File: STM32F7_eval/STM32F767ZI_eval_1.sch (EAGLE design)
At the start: 101 parts, among them CN3 GROVE-4P-CONN-I2C-90D, CN4 GROVE-4P-CONN-AN01-90D, CN5 ARDUINO_COMPAT_IF, CN6 STLINKV21_SWD_IF, CN7 WFT0750CZ09-SMD_, CN8 MCO_IF, CN9 UART_IF, Q1 PMF370XN_, SW1 SKRPACE010_, SW2 SKRPACE010_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

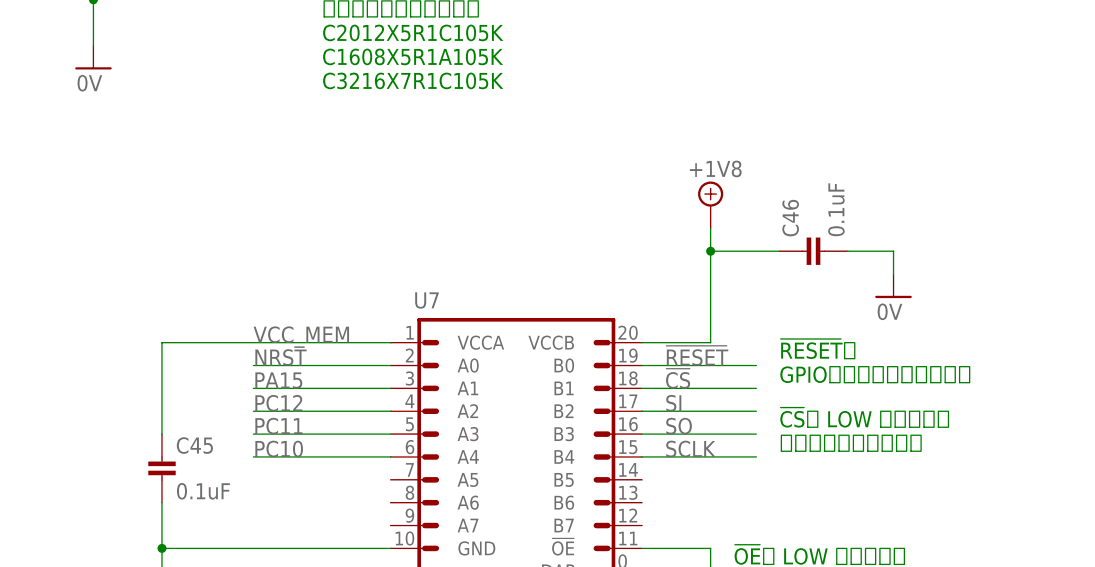
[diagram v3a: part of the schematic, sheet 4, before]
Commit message: 評価回路を修正
・コメント修正
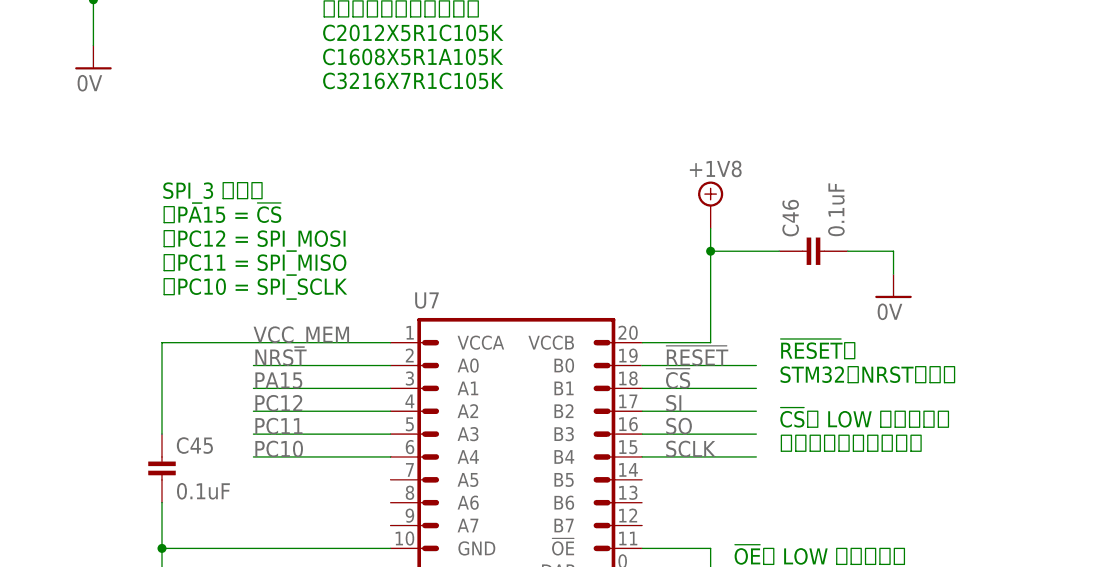
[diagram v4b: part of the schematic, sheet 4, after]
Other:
- note added: "!RESET!は STM32のNRSTに接続"
- note added: "I2C_2 を使用 ・PB10 = I2C_SCL ・PB11 = I2C_SDA"
- note added: "SPI_3 を使用 ・PA15 = !CS! ・PC12 = SPI_MOSI ・PC11 = SPI_MISO ・PC10 = SPI_SCLK"
- note removed: "!RESET!は GPIOを使用しても制御可能"
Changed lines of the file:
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@@
 <setting verticaltext="up"/>
 </settings>
-<grid distance="0.1" unitdist="inch" unit="inch" style="lines" multiple="1" display="no" altdistance="0.01" altunitdist="inch" altunit="inch"/>
+<grid distance="0.1" unitdist="inch" unit="inch" style="lines" multiple="1" display="yes" altdistance="0.01" altunitdist="inch" altunit="inch"/>
 <layers>
 <layer number="1" name="Top" color="4" fill="1" visible="no" active="no"/>
@@
 2.9inch - 1uF</text>
 <text x="101.6" y="165.1" size="2.54" layer="91">EPD接続インターフェース回路図</text>
+<text x="111.76" y="22.86" size="1.778" layer="91" align="top-left">I2C_2 を使用
+・PB10 = I2C_SCL
+・PB11 = I2C_SDA
+</text>
 </plain>
 <instances>
@@
 フラッシュが使用可能</text>
 <text x="200.66" y="83.82" size="1.778" layer="91" align="top-left">!RESET!は
-GPIOを使用しても制御可能</text>
+STM32のNRSTに接続</text>
 <text x="195.58" y="60.96" size="1.778" layer="91" align="top-left">!OE!に LOW を出力時は
 FXMA108のバスが
@@
 C3216X7R1C105K </text>
 <text x="104.14" y="160.02" size="2.54" layer="91">フラッシュメモリー回路図</text>
+<text x="132.08" y="101.6" size="1.778" layer="91" align="top-left">SPI_3 を使用
+・PA15 = !CS!
+・PC12 = SPI_MOSI
+・PC11 = SPI_MISO
+・PC10 = SPI_SCLK
+</text>
 </plain>
 <instances>

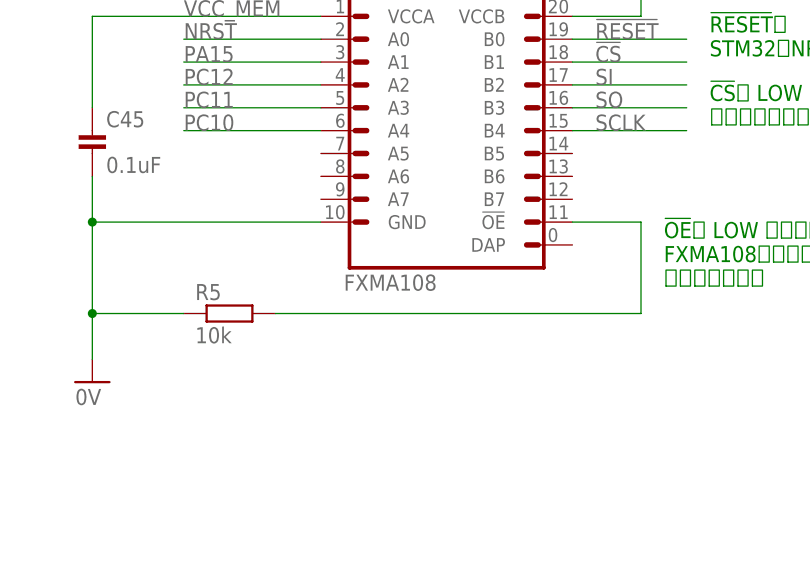
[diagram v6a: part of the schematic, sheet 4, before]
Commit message: 評価回路を修正
・手はんだパターンに置換え
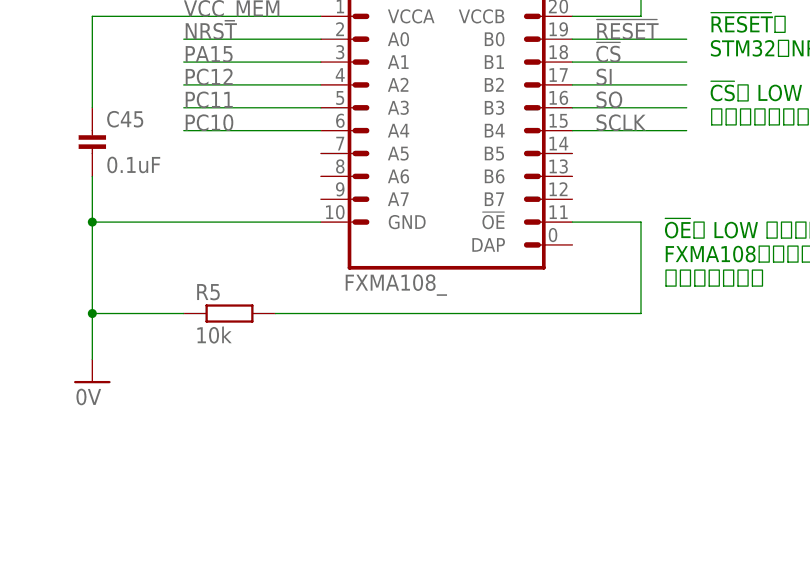
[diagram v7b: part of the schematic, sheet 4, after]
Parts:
- U7: value FXMA108 -> FXMA108_; device Parts:FXMA108 -> Parts:FXMA108_
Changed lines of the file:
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@@
 <part name="GND18" library="Supply" deviceset="0V" device=""/>
 <part name="C42" library="Parts" deviceset="CAP" device="_0603_DEV" value="0.1uF"/>
-<part name="U7" library="Parts" deviceset="FXMA108" device=""/>
+<part name="U7" library="Parts" deviceset="FXMA108" device="_" value="FXMA108_"/>
 <part name="SUPPLY1" library="PartsForProto" deviceset="+1V8" device=""/>
 <part name="SUPPLY2" library="PartsForProto" deviceset="+1V8" device=""/>

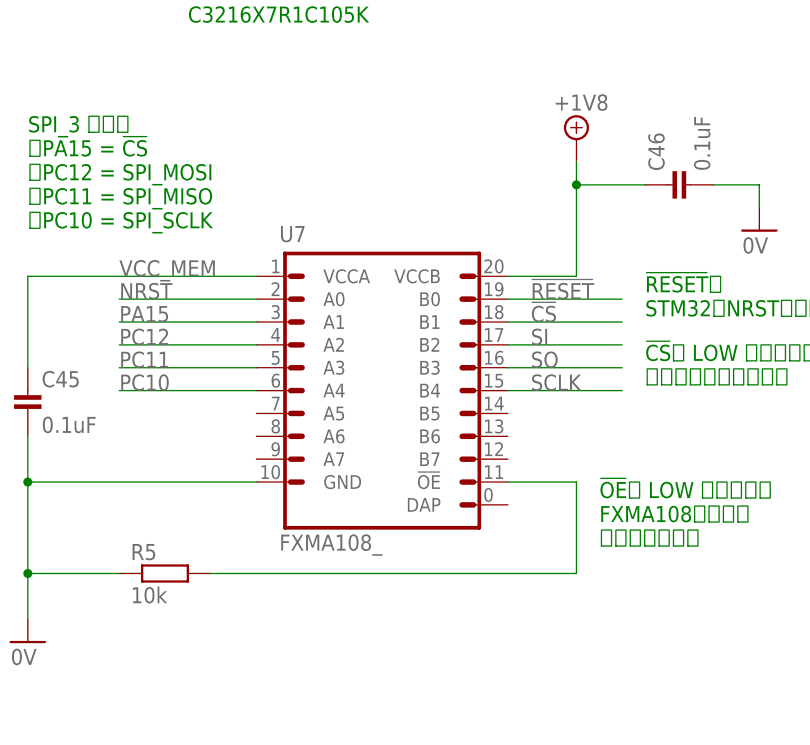
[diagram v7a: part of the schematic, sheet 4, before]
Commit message: 評価回路を修正
・配線を修正
・+1V8のNAMEが不正だったので修正
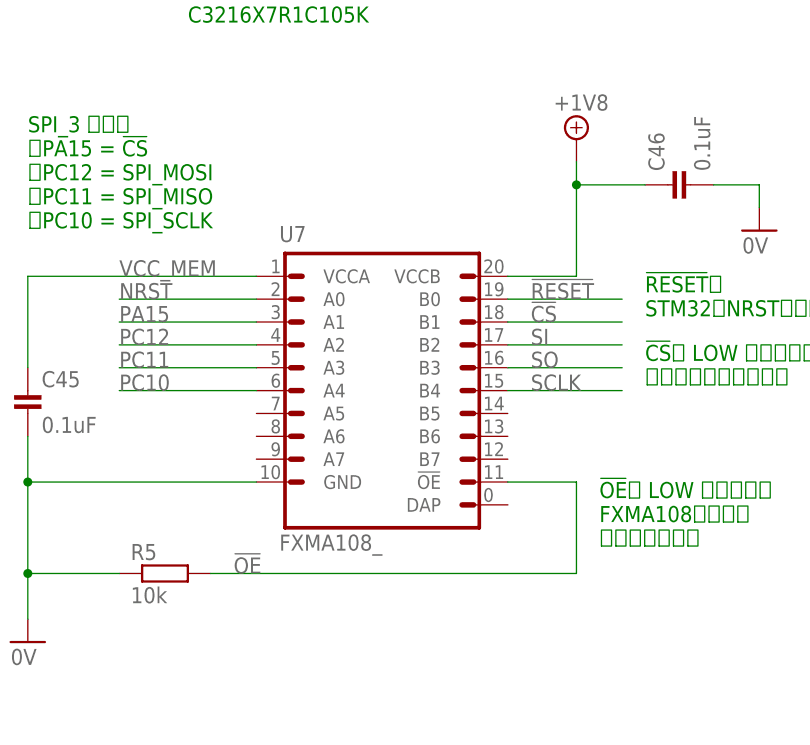
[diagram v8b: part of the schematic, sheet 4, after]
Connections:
- net +18V renamed +1V8
- net N$15 renamed !OE!
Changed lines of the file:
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@@
 <part name="C42" library="Parts" deviceset="CAP" device="_0603_DEV" value="0.1uF"/>
 <part name="U7" library="Parts" deviceset="FXMA108" device="_" value="FXMA108_"/>
-<part name="SUPPLY1" library="PartsForProto" deviceset="+1V8" device=""/>
-<part name="SUPPLY2" library="PartsForProto" deviceset="+1V8" device=""/>
+<part name="SUPPLY1" library="Supply" deviceset="+1V8" device=""/>
 <part name="GND20" library="Supply" deviceset="0V" device=""/>
-<part name="SUPPLY3" library="PartsForProto" deviceset="+1V8" device=""/>
+<part name="SUPPLY3" library="Supply" deviceset="+1V8" device=""/>
 <part name="GND21" library="Supply" deviceset="0V" device=""/>
 <part name="U8" library="Parts" deviceset="NCP563" device=""/>
@@
 <part name="+3V4" library="Supply" deviceset="+3V3" device=""/>
 <part name="R26" library="Parts" deviceset="RESISTOR" device="_0603_DEV" value="0"/>
+<part name="SUPPLY2" library="Supply" deviceset="+1V8" device=""/>
 </parts>
 <sheets>
@@
 <instance part="C42" gate="G$1" x="93.98" y="63.5"/>
 <instance part="U7" gate="G$1" x="157.48" y="83.82"/>
-<instance part="SUPPLY1" gate="+18V" x="93.98" y="93.98"/>
-<instance part="SUPPLY2" gate="+18V" x="193.04" y="99.06"/>
+<instance part="SUPPLY1" gate="G$1" x="93.98" y="93.98"/>
 <instance part="GND20" gate="1" x="132.08" y="43.18"/>
-<instance part="SUPPLY3" gate="+18V" x="147.32" y="149.86"/>
+<instance part="SUPPLY3" gate="G$1" x="147.32" y="149.86"/>
 <instance part="GND21" gate="1" x="124.46" y="114.3"/>
 <instance part="U8" gate="G$1" x="116.84" y="144.78"/>
@@
 <instance part="R25" gate="G$1" x="71.12" y="139.7"/>
 <instance part="+3V4" gate="G$1" x="66.04" y="152.4"/>
+<instance part="SUPPLY2" gate="G$1" x="193.04" y="99.06"/>
 </instances>
 <busses>
@@
 </segment>
 </net>
-<net name="+18V" class="0">
-<segment>
-<pinref part="U7" gate="G$1" pin="VCCB"/>
-<wire x1="185.42" y1="83.82" x2="193.04" y2="83.82" width="0.1524" layer="91"/>
-<pinref part="SUPPLY2" gate="+18V" pin="+18V"/>
-<wire x1="193.04" y1="83.82" x2="193.04" y2="93.98" width="0.1524" layer="91"/>
-<pinref part="C46" gate="G$1" pin="1"/>
-<wire x1="193.04" y1="93.98" x2="193.04" y2="96.52" width="0.1524" layer="91"/>
-<wire x1="193.04" y1="93.98" x2="200.66" y2="93.98" width="0.1524" layer="91"/>
-<junction x="193.04" y="93.98"/>
-</segment>
-<segment>
-<pinref part="U6" gate="G$1" pin="VCC"/>
-<wire x1="88.9" y1="76.2" x2="93.98" y2="76.2" width="0.1524" layer="91"/>
-<wire x1="93.98" y1="76.2" x2="93.98" y2="86.36" width="0.1524" layer="91"/>
-<pinref part="C42" gate="G$1" pin="1"/>
-<wire x1="93.98" y1="86.36" x2="93.98" y2="91.44" width="0.1524" layer="91"/>
-<wire x1="93.98" y1="76.2" x2="93.98" y2="63.5" width="0.1524" layer="91"/>
-<junction x="93.98" y="76.2"/>
-<pinref part="SUPPLY1" gate="+18V" pin="+18V"/>
-<pinref part="U6" gate="G$1" pin="!WP!/SIO2"/>
-<wire x1="55.88" y1="71.12" x2="43.18" y2="71.12" width="0.1524" layer="91"/>
-<wire x1="43.18" y1="71.12" x2="43.18" y2="86.36" width="0.1524" layer="91"/>
-<wire x1="43.18" y1="86.36" x2="93.98" y2="86.36" width="0.1524" layer="91"/>
-<junction x="93.98" y="86.36"/>
-</segment>
-<segment>
-<pinref part="U8" gate="G$1" pin="VOUT"/>
-<pinref part="SUPPLY3" gate="+18V" pin="+18V"/>
-<wire x1="139.7" y1="139.7" x2="147.32" y2="139.7" width="0.1524" layer="91"/>
-<wire x1="147.32" y1="139.7" x2="147.32" y2="147.32" width="0.1524" layer="91"/>
-<pinref part="C44" gate="G$1" pin="1"/>
-<wire x1="147.32" y1="139.7" x2="147.32" y2="134.62" width="0.1524" layer="91"/>
-<junction x="147.32" y="139.7"/>
-</segment>
-</net>
 <net name="!RESET!" class="0">
 <segment>
@@
 </segment>
 </net>
-<net name="N$15" class="0">
+<net name="!OE!" class="0">
 <segment>
 <pinref part="R5" gate="G$1" pin="2"/>
@@
 <pinref part="U7" gate="G$1" pin="!OE!"/>
 <wire x1="193.04" y1="60.96" x2="185.42" y2="60.96" width="0.1524" layer="91"/>
+<label x="154.94" y="50.8" size="1.778" layer="95"/>
 </segment>
 </net>
@@
 </segment>
 </net>
+<net name="+1V8" class="0">
+<segment>
+<pinref part="U6" gate="G$1" pin="VCC"/>
+<wire x1="88.9" y1="76.2" x2="93.98" y2="76.2" width="0.1524" layer="91"/>
+<wire x1="93.98" y1="76.2" x2="93.98" y2="86.36" width="0.1524" layer="91"/>
+<pinref part="C42" gate="G$1" pin="1"/>
+<wire x1="93.98" y1="86.36" x2="93.98" y2="91.44" width="0.1524" layer="91"/>
+<wire x1="93.98" y1="76.2" x2="93.98" y2="63.5" width="0.1524" layer="91"/>
+<junction x="93.98" y="76.2"/>
+<pinref part="SUPPLY1" gate="G$1" pin="+1V8"/>
+<pinref part="U6" gate="G$1" pin="!WP!/SIO2"/>
+<wire x1="55.88" y1="71.12" x2="43.18" y2="71.12" width="0.1524" layer="91"/>
+<wire x1="43.18" y1="71.12" x2="43.18" y2="86.36" width="0.1524" layer="91"/>
+<wire x1="43.18" y1="86.36" x2="93.98" y2="86.36" width="0.1524" layer="91"/>
+<junction x="93.98" y="86.36"/>
+</segment>
+<segment>
+<pinref part="U8" gate="G$1" pin="VOUT"/>
+<pinref part="SUPPLY3" gate="G$1" pin="+1V8"/>
+<wire x1="139.7" y1="139.7" x2="147.32" y2="139.7" width="0.1524" layer="91"/>
+<wire x1="147.32" y1="139.7" x2="147.32" y2="147.32" width="0.1524" layer="91"/>
+<pinref part="C44" gate="G$1" pin="1"/>
+<wire x1="147.32" y1="139.7" x2="147.32" y2="134.62" width="0.1524" layer="91"/>
+<junction x="147.32" y="139.7"/>
+</segment>
+<segment>
+<pinref part="U7" gate="G$1" pin="VCCB"/>
+<wire x1="185.42" y1="83.82" x2="193.04" y2="83.82" width="0.1524" layer="91"/>
+<wire x1="193.04" y1="83.82" x2="193.04" y2="93.98" width="0.1524" layer="91"/>
+<pinref part="C46" gate="G$1" pin="1"/>
+<wire x1="193.04" y1="93.98" x2="200.66" y2="93.98" width="0.1524" layer="91"/>
+<pinref part="SUPPLY2" gate="G$1" pin="+1V8"/>
+<wire x1="193.04" y1="96.52" x2="193.04" y2="93.98" width="0.1524" layer="91"/>
+<junction x="193.04" y="93.98"/>
+</segment>
+</net>
